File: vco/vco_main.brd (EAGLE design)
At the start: 94.9 x 107.9 mm, 101 parts, among them IC1 OPA4130U, IC2 LM13700M, IC3 OPA4130U, IC4 OPA4130U, Q1 MMBFJ3

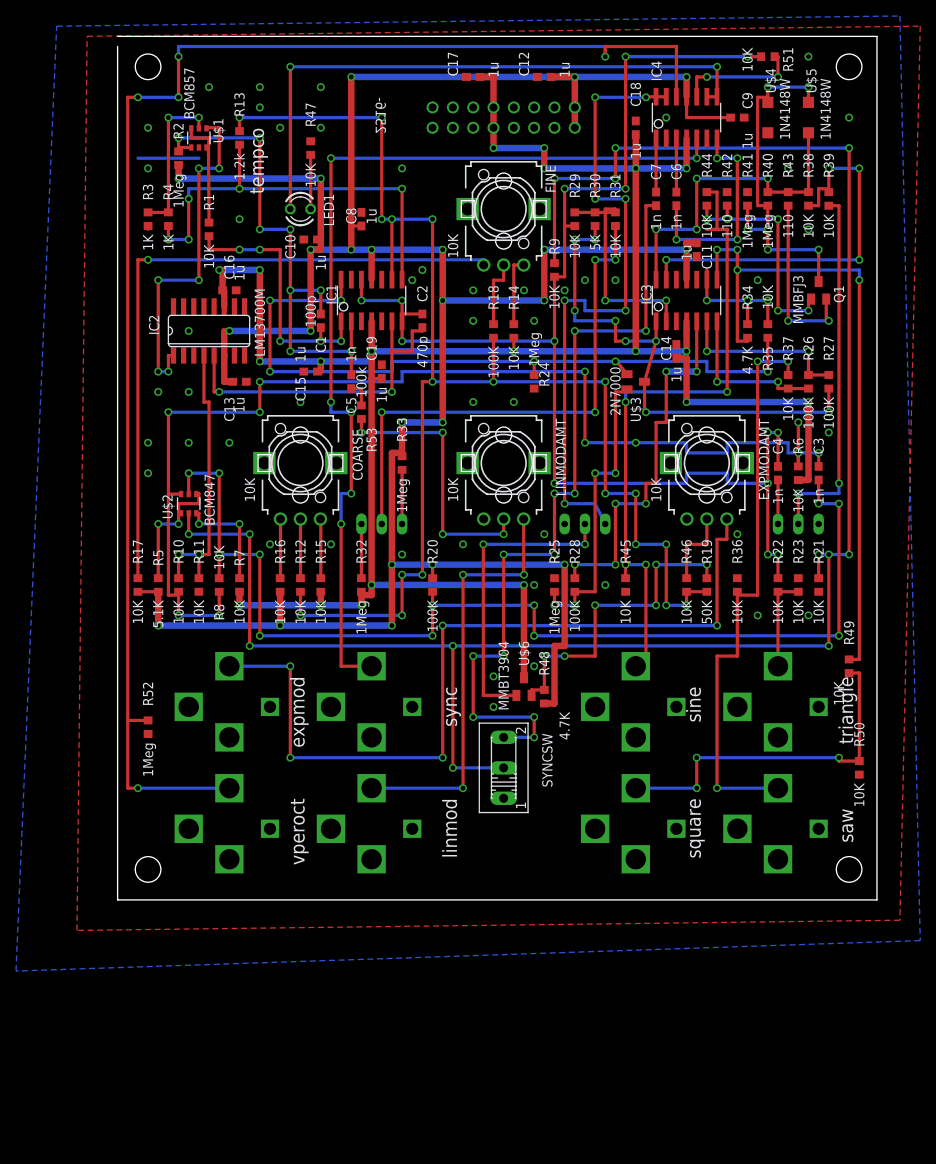
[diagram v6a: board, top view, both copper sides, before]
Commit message: fixed a serious problem with the saw.  cleaned some nets up.
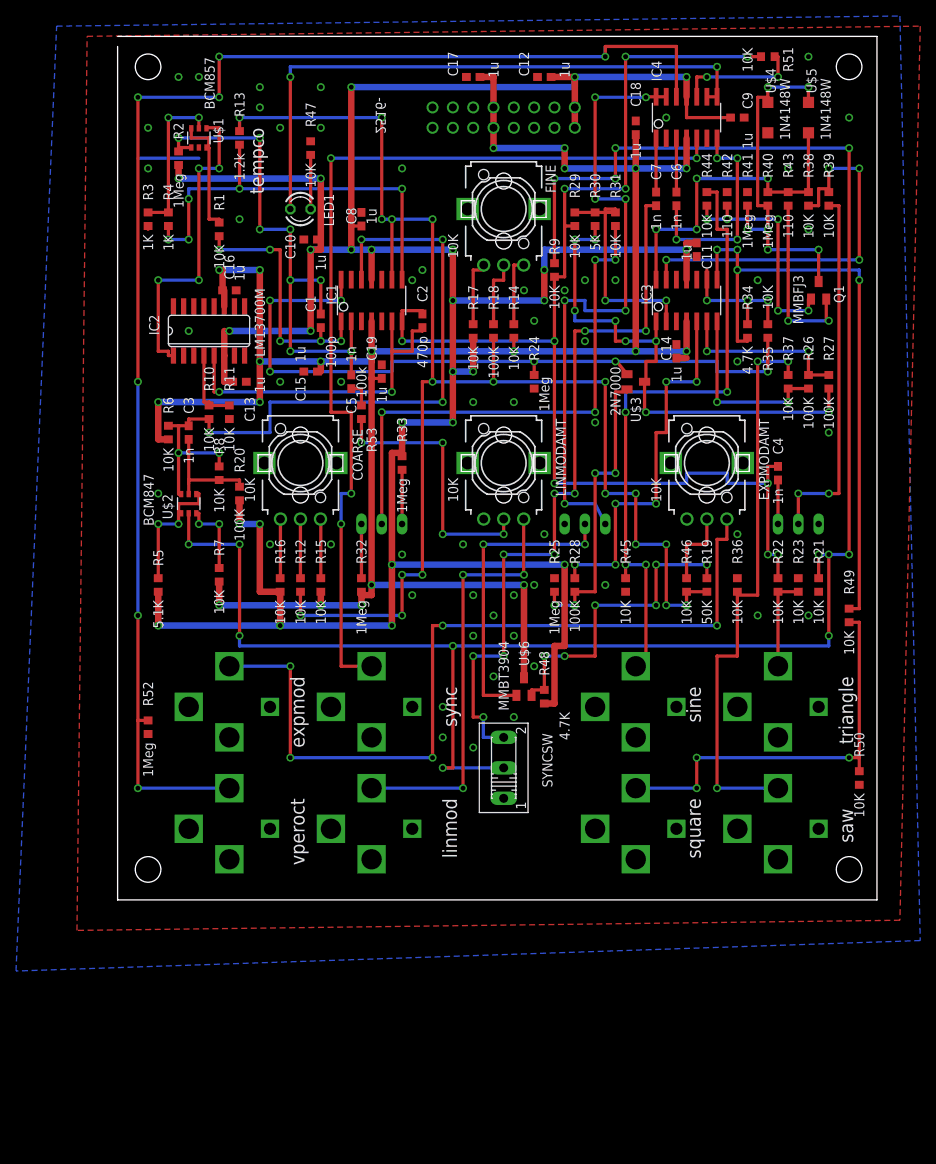
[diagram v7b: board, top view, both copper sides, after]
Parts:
- moved R6 78.9 mm to (6.35, 58.4)
- moved C3 78.9 mm to (8.89, 58.4)
- moved R17 52.6 mm to (44.5, 71.1)
- moved R20 26.7 mm to (15.2, 50.8), turned to 90 degrees
- moved R10 21.9 mm to (11.4, 61.0)
- moved R11 21.9 mm to (14.0, 61.0)
- moved R8 14.0 mm to (12.7, 53.3), turned to 270 degrees
- moved R49 6.35 mm to (91.4, 35.6)
- moved R7 2.84 mm to (12.7, 40.6)
- moved R50 1.27 mm to (92.7, 15.2)
- moved R1 1.27 mm to (12.7, 83.8)
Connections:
- removed net N$12: C3.2, R10.2, R6.1, R8.1, U$2.6
- new net TOSQU: C3.2, IC1.12, R10.2, R6.1, R8.1, U$2.6
- net TRI: no longer IC1.12
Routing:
- net N$12: track 145.1 -> 0.00 mm, vias 11 -> 0
- net N$4: track 138.5 -> 14.0 mm, vias 12 -> 0
- net TOSQU: track 0.00 -> 91.8 mm, vias 0 -> 6
- net N$20: track 83.7 -> 8.70 mm, vias 1 -> 0
- net N$14: track 35.2 -> 9.41 mm, vias 2 -> 0
- net -12V: track 343.2 -> 363.9 mm, vias 23 -> 26
- net TRI: track 169.0 -> 152.0 mm, vias 14 -> 10
- net N$51: track 100.8 -> 93.1 mm, vias 11 -> 9
- net N$9: track 44.4 -> 51.6 mm
- net N$36: track 84.6 -> 78.2 mm
- net N$54: track 185.4 -> 180.3 mm, vias 5 -> 7
- net +12V: track 273.5 -> 269.3 mm
- net IABC: track 43.7 -> 39.7 mm, vias 6 -> 4
- net N$23: track 13.5 -> 9.70 mm
- net N$27: track 19.8 -> 23.2 mm
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
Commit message: cleaned up the layout a bit.  fixed component values.
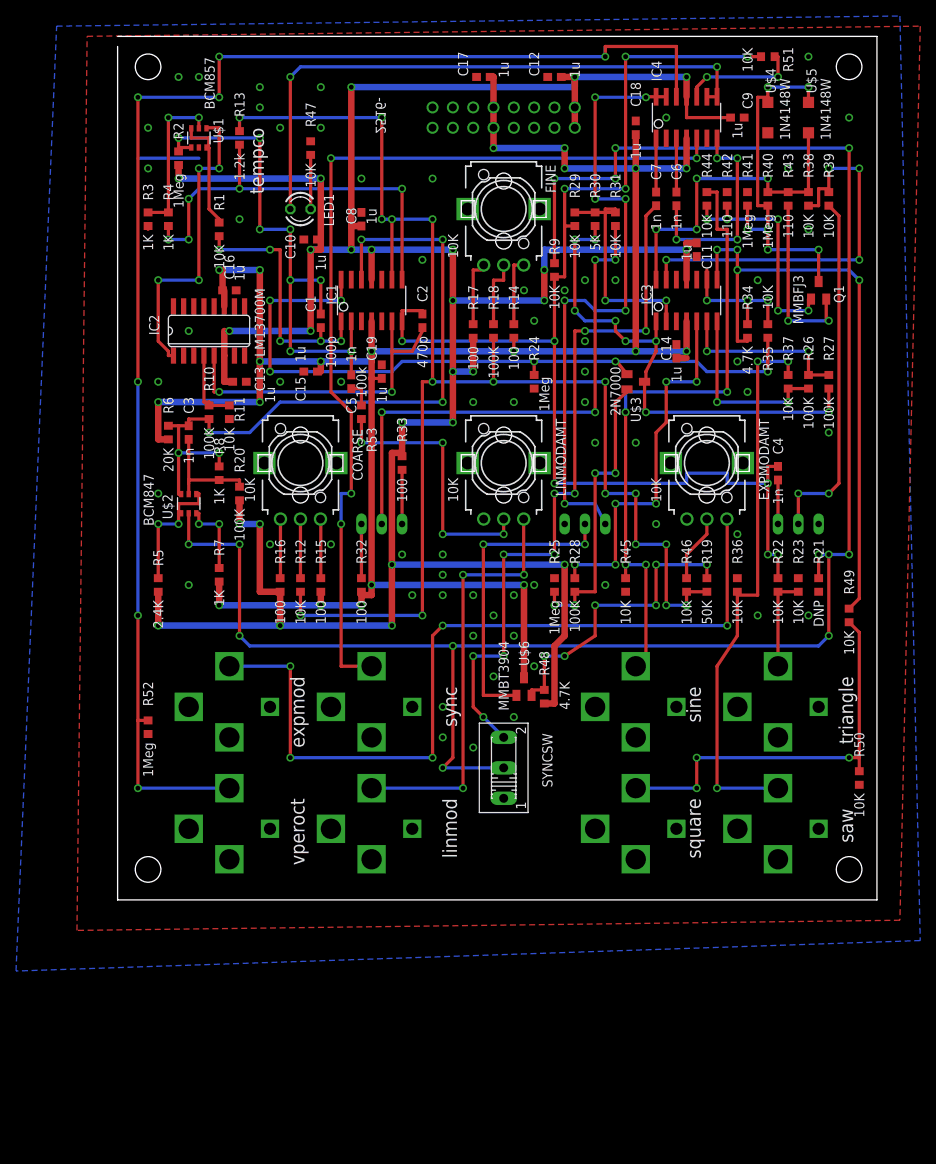
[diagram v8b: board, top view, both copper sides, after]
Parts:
- R10: value 10K -> 100K
- R14, R15, R16, R17: value 10K -> 100
- R21: value 10K -> DNP
- R32, R33: value 1Meg -> 100
- R5: value 5.1K -> 2.4K
- R6: value 10K -> 20K
- R7, R8: value 10K -> 1K
- moved C12 1.27 mm to (54.6, 102.9)
- moved C17 1.27 mm to (45.7, 102.9)
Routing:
- net N$51: track 93.1 -> 90.2 mm
- net N$28: track 65.9 -> 63.4 mm
- net TOSQU: track 91.8 -> 89.5 mm
- net SYNC: track 240.9 -> 238.7 mm
- net -12V: track 363.9 -> 361.9 mm
- net N$22: track 39.9 -> 38.2 mm
- net N$33: track 72.4 -> 70.6 mm
- net N$39: track 46.1 -> 44.7 mm
- net N$42: track 9.93 -> 8.44 mm
- net N$57: track 93.3 -> 91.8 mm
- net N$36: track 78.2 -> 76.8 mm
- net N$50: track 119.4 -> 117.9 mm
- net +12V: track 269.3 -> 268.0 mm
- net N$19: track 42.4 -> 41.4 mm
- net N$10: track 37.7 -> 37.0 mm
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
